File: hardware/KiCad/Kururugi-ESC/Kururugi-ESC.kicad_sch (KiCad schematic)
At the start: 77 parts, among them J1 Conn_01x01, J2 Conn_01x01, J3 Conn_01x01, J4 Conn_01x01, J5 Conn_01x01, J6 JTAG_TC2030, J7 Conn_01x01, J8 Conn_01x01, U1 STM32G484CEU6, U2 LM5160A, U3 TPS7B92033, X1 16MHz

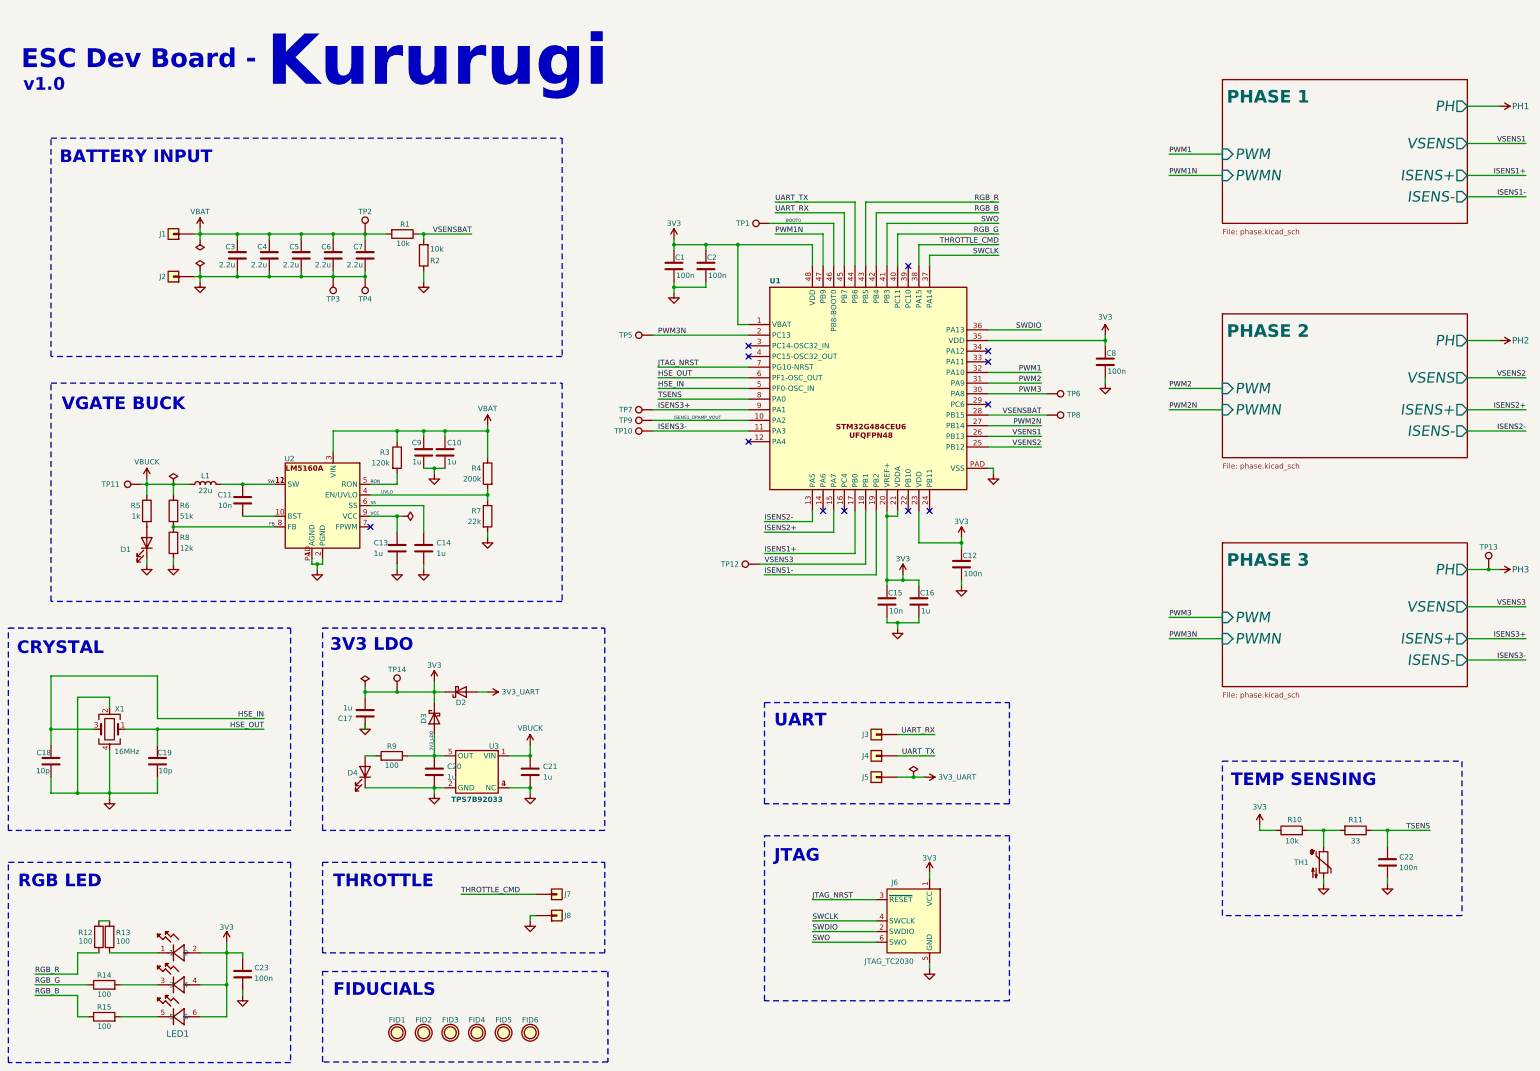
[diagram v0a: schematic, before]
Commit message: Doc Update + Added CubeIDE
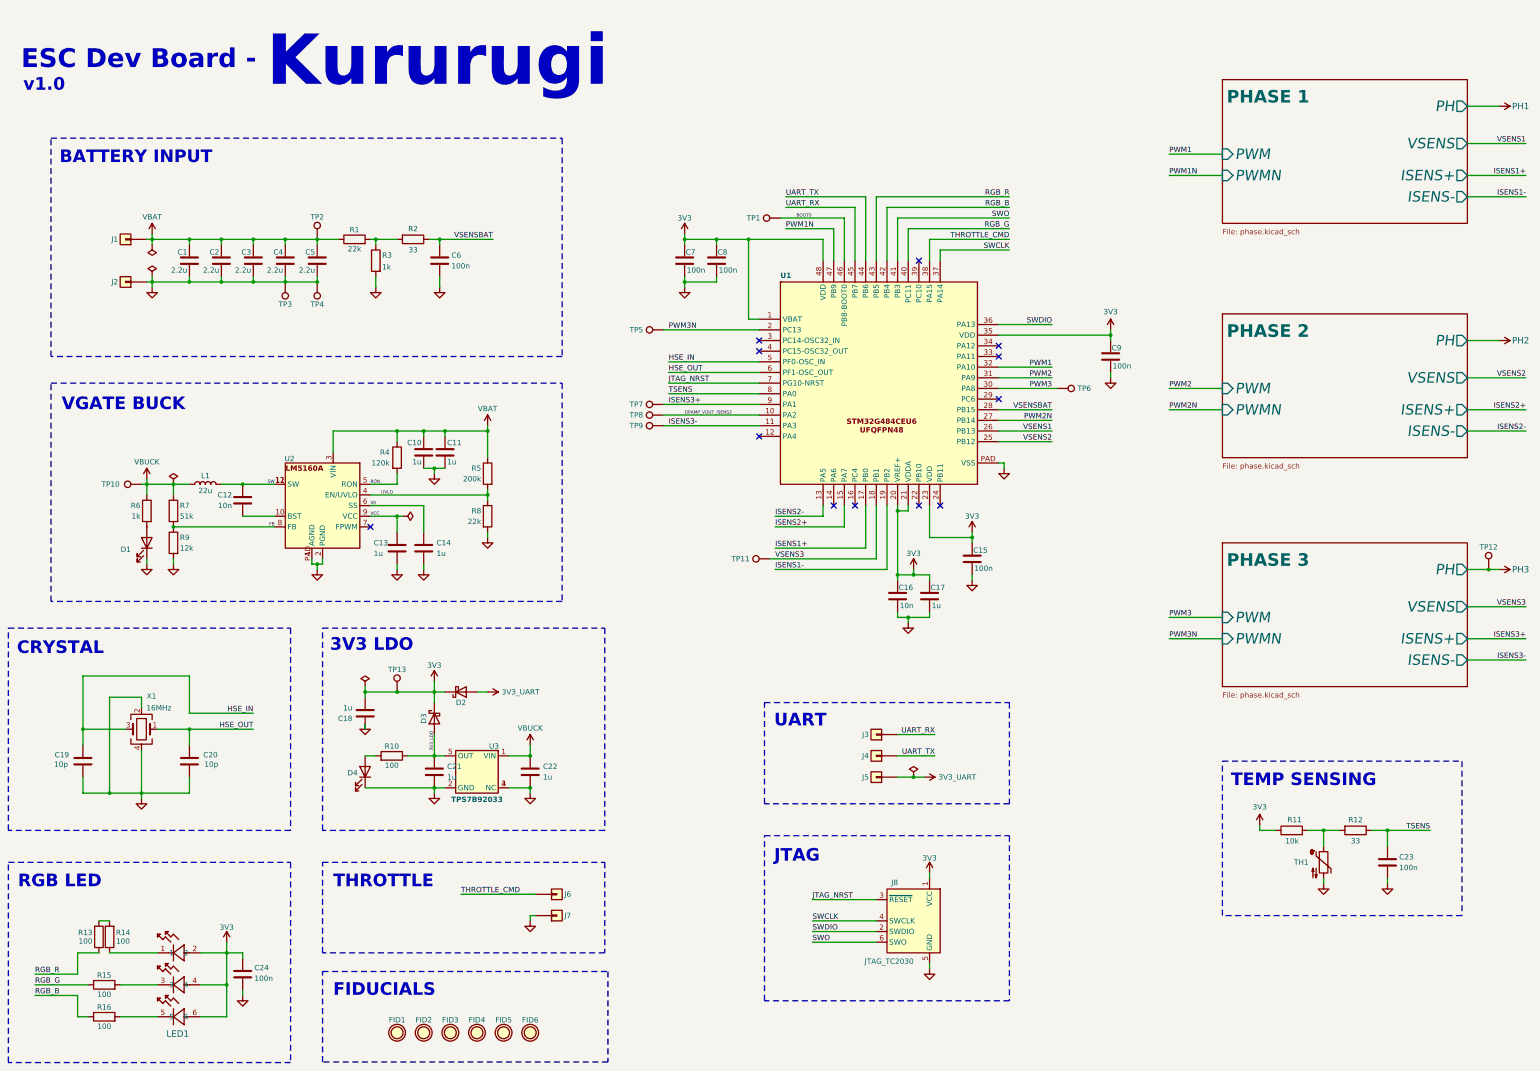
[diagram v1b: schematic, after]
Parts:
- removed R1: 10k, KururugiESC-Footprints-Lib:R_0402_1005Metric, symbol KururugiESC-Symbols-Lib:0402WGF1002TCE
- removed TP8: TestPoint, KururugiESC-Footprints-Lib:TestPoint_Pad_D1.0mm, symbol KururugiESC-Symbols-Lib:TestPoint
- added C6: 100n, KururugiESC-Footprints-Lib:C_0402_1005Metric, symbol KururugiESC-Symbols-Lib:CL05B104KO5NNNC
- added R1: 22k, KururugiESC-Footprints-Lib:R_0402_1005Metric, symbol KururugiESC-Symbols-Lib:0402WGF2202TCE
- added R2: 33, KururugiESC-Footprints-Lib:R_0402_1005Metric, symbol KururugiESC-Symbols-Lib:0402WGF330JTCE
- R3: renamed from R2; value 10k -> 1k; symbol KururugiESC-Symbols-Lib:0402WGF1002TCE -> KururugiESC-Symbols-Lib:0402WGF1001TCE; Distributor Link 1 https://www.mouser.com/ProductDetail/Royalohm/0402WGF1002TC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 -> https://www.lcsc.com/product-detail/C11702.html; Distributor Link 2 (none) -> https://www.mouser.com/ProductDetail/Royalohm/0402WGF1002TC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; LCSC C25744 -> C11702; Manufacturer Part Number 0402WGF1002TCE -> 0402WGF1001TCE
- renumbered C3 to C1, C9 to C10, C10 to C11, C11 to C12, C12 to C15, C15 to C16, C16 to C17, C17 to C18, C18 to C19, C4 to C2, C19 to C20, C20 to C21, C21 to C22, C22 to C23, C23 to C24, C5 to C3, C6 to C4, C7 to C5, C1 to C7, C2 to C8, C8 to C9, J7 to J6, J8 to J7, J6 to J8, R9 to R10, R10 to R11, R11 to R12, R12 to R13, R13 to R14, R14 to R15, R15 to R16, R3 to R4, R4 to R5, R5 to R6, R6 to R7, R7 to R8, R8 to R9, TP11 to TP10, TP12 to TP11, TP13 to TP12, TP14 to TP13, TP9 to TP8, TP10 to TP9
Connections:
- net GND: now also R3.2, C6.2; no longer R3.1
- net VBAT: now also R1.1
- net VSENSBAT: now also C6.1, R2.1; no longer R3.2
- net ISENS1_OPAMP_VOUT renamed OPAMP_VOUT_ISENS3
- new net: R1.2, R2.2, R3.1
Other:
- moved on the sheet: C1, C15, C16, C17, C19, C2, C20, C3, C4, C5, C7, C8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

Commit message: Kicad minor corrections
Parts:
- R12, R2: LCSC C25752 -> C25105
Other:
- moved on the sheet: C15, C16, C17, C7, C8, C9, J6, J7, TP1, TP11, TP5, TP6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
